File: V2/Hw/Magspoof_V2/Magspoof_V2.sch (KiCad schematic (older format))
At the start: 16 parts

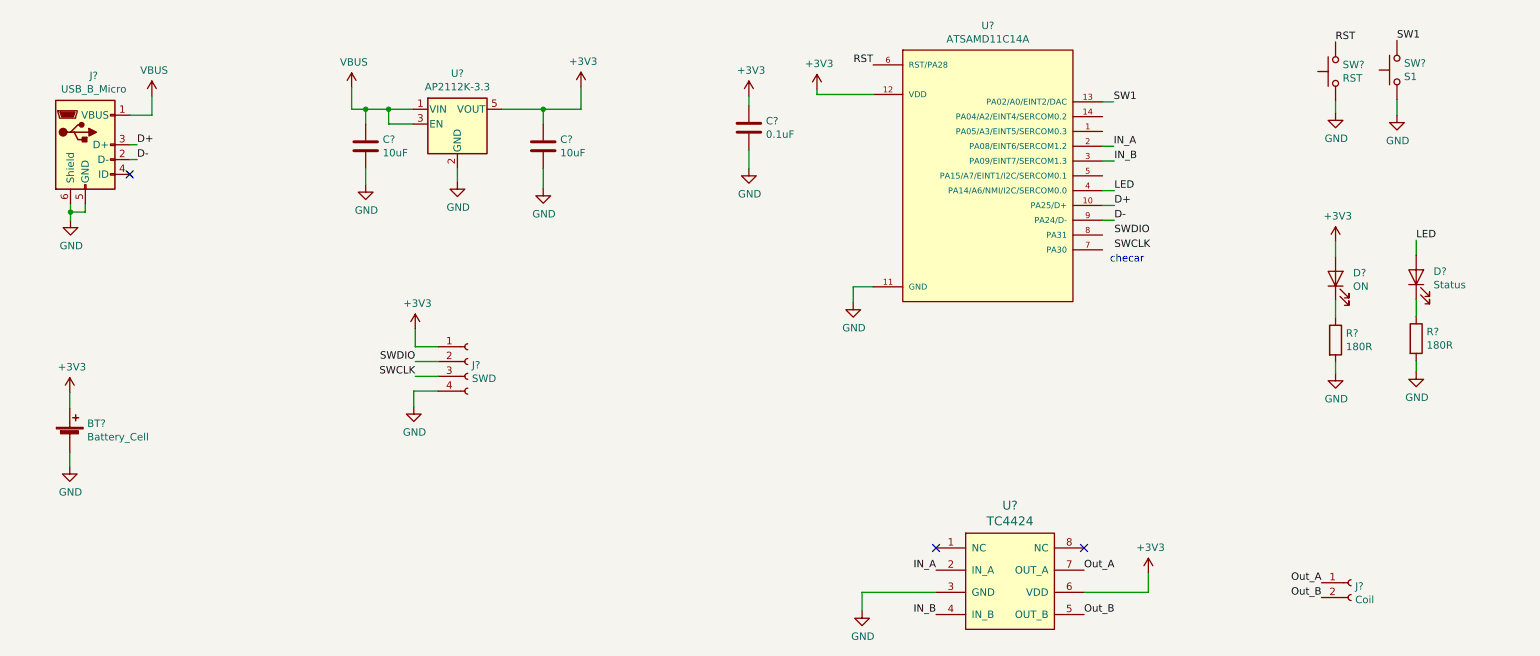
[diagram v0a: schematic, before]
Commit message: Add foortprints and first route
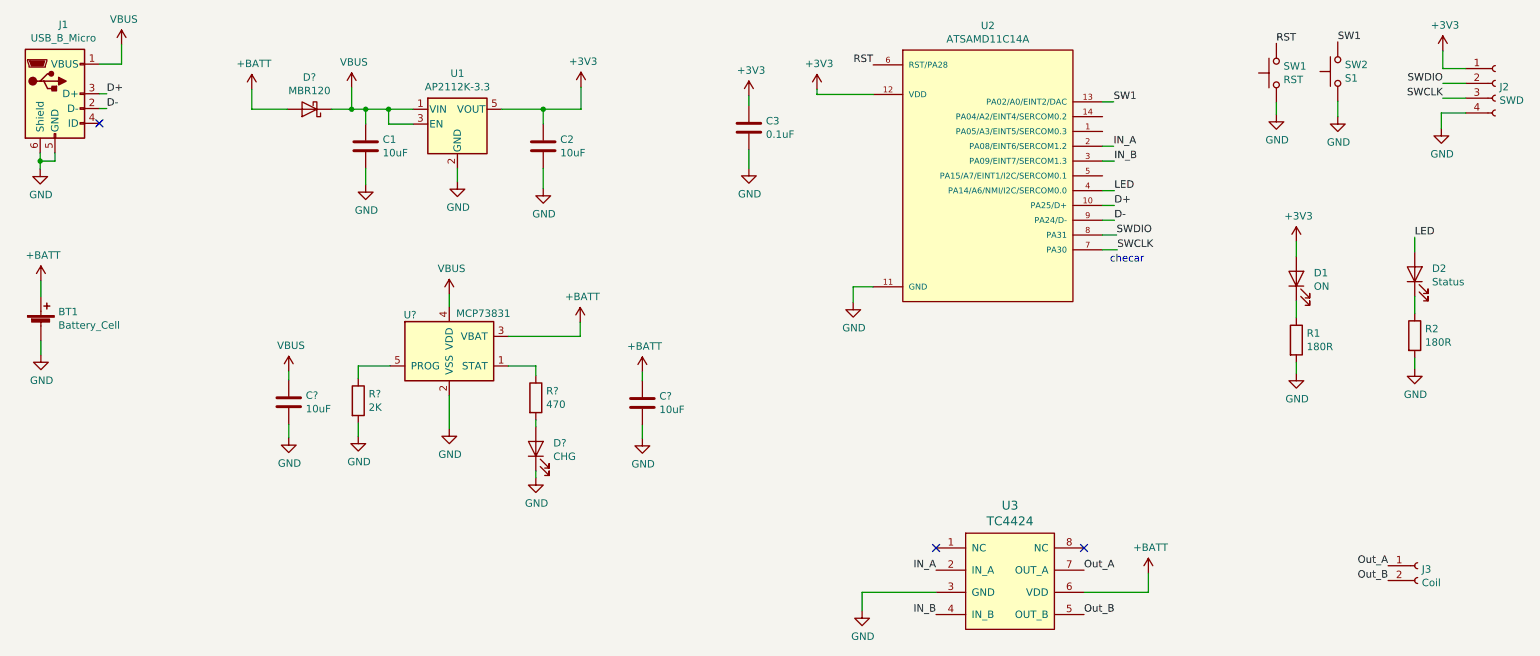
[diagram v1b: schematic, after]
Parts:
- added C? (x2): 10uF, Capacitor_SMD:C_0805_2012Metric_Pad1.15x1.40mm_HandSolder, symbol Device:C
- added D?: MBR120, Diode_SMD:D_SOD-123, symbol Device:D_Schottky
- added D?: CHG, LED_SMD:LED_0805_2012Metric_Pad1.15x1.40mm_HandSolder, symbol Device:LED
- added R?: 2K, Resistor_SMD:R_0805_2012Metric_Pad1.15x1.40mm_HandSolder, symbol Device:R
- added R?: 470, Resistor_SMD:R_0805_2012Metric_Pad1.15x1.40mm_HandSolder, symbol Device:R
- added U?: MCP73831, Package_TO_SOT_SMD:SOT-23-5, symbol Battery_Management:MCP73831-2-OT
- BT1: renamed from BT?; footprint (none) -> Connector_PinHeader_2.54mm:PinHeader_1x02_P2.54mm_Vertical
- C1, C2, C3: renamed from C?; footprint (none) -> Capacitor_SMD:C_0805_2012Metric_Pad1.15x1.40mm_HandSolder
- D1, D2: renamed from D?; footprint (none) -> LED_SMD:LED_0805_2012Metric_Pad1.15x1.40mm_HandSolder
- J1: renamed from J?; footprint (none) -> USB:629105150521
- J2: renamed from J?; footprint (none) -> Connector_PinHeader_2.54mm:PinHeader_1x04_P2.54mm_Vertical
- J3: renamed from J?; footprint (none) -> Connector_PinHeader_2.54mm:PinHeader_1x02_P2.54mm_Vertical
- R1, R2: renamed from R?; footprint (none) -> Resistor_SMD:R_0805_2012Metric_Pad1.15x1.40mm_HandSolder
- SW1, SW2: renamed from SW?; footprint (none) -> Button_Switch_SMD:SW_SPST_TL3342
- gave numbers to parts that had none: 3
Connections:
- net +3V3: no longer BT1.1 (+), U3.6 (VDD)
- net GND: now also C?.2, C?.2, D?.1 (K), R?.2, U?.2 (VSS)
- net SWCLK: now also U2.7 (PA30)
- net SWDIO: now also U2.8 (PA31)
- net VBUS: now also C?.1, D?.1 (K), U?.4 (VDD)
- new net: R?.1, U?.1 (STAT)
- new net: R?.1, U?.5 (PROG)
- new net: D?.2 (A), R?.2
- new net +BATT: BT1.1 (+), C?.1, D?.2 (A), U3.6 (VDD), U?.3 (VBAT)
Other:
- moved on the sheet: BT1, D1, D2, J1, J2, J3, R1, R2, SW1, SW2

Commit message: Update desing
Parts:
- added D5: MBR120, Diode_SMD:D_SOD-123, symbol Device:D_Schottky
- gave numbers to parts that had none: 7
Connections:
- net +BATT: now also D5.1 (K); no longer BT1.1 (+)
- new net: BT1.1 (+), D5.2 (A)
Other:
- moved on the sheet: BT1
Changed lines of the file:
@@
 L Device:Battery_Cell BT1
 U 1 1 5D60DD69
-P 960 2880
-F 0 "BT1" H 1078 2976 50  0000 L CNN
-F 1 "Battery_Cell" H 1078 2885 50  0000 L CNN
-F 2 "Connector_PinHeader_2.54mm:PinHeader_1x02_P2.54mm_Vertical" V 960 2940 50  0001 C CNN
-F 3 "~" V 960 2940 50  0001 C CNN
-	1    960  2880
+P 1030 3315
+F 0 "BT1" H 1148 3411 50  0000 L CNN
+F 1 "Battery_Cell" H 1148 3320 50  0000 L CNN
+F 2 "Connector_PinHeader_2.54mm:PinHeader_1x02_P2.54mm_Vertical" V 1030 3375 50  0001 C CNN
+F 3 "~" V 1030 3375 50  0001 C CNN
+	1    1030 3315
 	1    0    0    -1
 $EndComp
@@
 L power:GND #PWR0104
 U 1 1 5D62366E
-P 960 3075
-F 0 "#PWR0104" H 960 2825 50  0001 C CNN
-F 1 "GND" H 965 2902 50  0000 C CNN
-F 2 "" H 960 3075 50  0001 C CNN
-F 3 "" H 960 3075 50  0001 C CNN
-	1    960  3075
-	1    0    0    -1
-$EndComp
-Wire Wire Line
-	960  3075 960  2980
+P 1030 3510
+F 0 "#PWR0104" H 1030 3260 50  0001 C CNN
+F 1 "GND" H 1035 3337 50  0000 C CNN
+F 2 "" H 1030 3510 50  0001 C CNN
+F 3 "" H 1030 3510 50  0001 C CNN
+	1    1030 3510
+	1    0    0    -1
+$EndComp
+Wire Wire Line
+	1030 3510 1030 3415
 $Comp
 L power:GND #PWR0105
@@
 	4355 1950 4355 1815
 Wire Wire Line
-	960  2575 960  2680
+	1030 3010 1030 3115
 $Comp
 L power:+3V3 #PWR0112
@@
 	8230 2265 8135 2265
 $Comp
-L Battery_Management:MCP73831-2-OT U?
+L Battery_Management:MCP73831-2-OT U4
 U 1 1 5D644F3C
 P 3720 3050
-F 0 "U?" H 3455 3295 50  0000 C CNN
+F 0 "U4" H 3455 3295 50  0000 C CNN
 F 1 "MCP73831" H 3950 3305 50  0000 C CNN
 F 2 "Package_TO_SOT_SMD:SOT-23-5" H 3770 2800 50  0001 L CIN
@@
 $EndComp
 $Comp
-L power:+BATT #PWR?
+L power:+BATT #PWR0111
 U 1 1 5D647CAB
-P 960 2575
-F 0 "#PWR?" H 960 2425 50  0001 C CNN
-F 1 "+BATT" H 975 2748 50  0000 C CNN
-F 2 "" H 960 2575 50  0001 C CNN
-F 3 "" H 960 2575 50  0001 C CNN
-	1    960  2575
-	1    0    0    -1
-$EndComp
-$Comp
-L power:+BATT #PWR?
+P 1030 2650
+F 0 "#PWR0111" H 1030 2500 50  0001 C CNN
+F 1 "+BATT" H 1045 2823 50  0000 C CNN
+F 2 "" H 1030 2650 50  0001 C CNN
+F 3 "" H 1030 2650 50  0001 C CNN
+	1    1030 2650
+	1    0    0    -1
+$EndComp
+$Comp
+L power:+BATT #PWR0113
 U 1 1 5D649416
 P 4605 2855
-F 0 "#PWR?" H 4605 2705 50  0001 C CNN
+F 0 "#PWR0113" H 4605 2705 50  0001 C CNN
 F 1 "+BATT" H 4620 3028 50  0000 C CNN
 F 2 "" H 4605 2855 50  0001 C CNN
@@
 	4605 2950 4120 2950
 $Comp
-L Device:D_Schottky D?
+L Device:D_Schottky D3
 U 1 1 5D64EF3A
 P 2775 1415
-F 0 "D?" H 2775 1199 50  0000 C CNN
+F 0 "D3" H 2775 1199 50  0000 C CNN
 F 1 "MBR120" H 2775 1290 50  0000 C CNN
 F 2 "Diode_SMD:D_SOD-123" H 2775 1415 50  0001 C CNN
@@
 Connection ~ 3060 1415
 $Comp
-L power:+BATT #PWR?
+L power:+BATT #PWR0123
 U 1 1 5D6508CA
 P 2385 1280
-F 0 "#PWR?" H 2385 1130 50  0001 C CNN
+F 0 "#PWR0123" H 2385 1130 50  0001 C CNN
 F 1 "+BATT" H 2400 1453 50  0000 C CNN
 F 2 "" H 2385 1280 50  0001 C CNN
@@
 	2385 1415 2625 1415
 $Comp
-L power:+BATT #PWR?
+L power:+BATT #PWR0124
 U 1 1 5D6528AA
 P 8445 4550
-F 0 "#PWR?" H 8445 4400 50  0001 C CNN
+F 0 "#PWR0124" H 8445 4400 50  0001 C CNN
 F 1 "+BATT" H 8460 4723 50  0000 C CNN
 F 2 "" H 8445 4550 50  0001 C CNN
@@
 $EndComp
 $Comp
-L Device:R R?
+L Device:R R3
 U 1 1 5D6565D3
 P 3105 3385
-F 0 "R?" H 3175 3431 50  0000 L CNN
+F 0 "R3" H 3175 3431 50  0000 L CNN
 F 1 "2K" H 3175 3340 50  0000 L CNN
 F 2 "Resistor_SMD:R_0805_2012Metric_Pad1.15x1.40mm_HandSolder" V 3035 3385 50  0001 C CNN
@@
 	3105 3150 3105 3235
 $Comp
-L power:GND #PWR?
+L power:GND #PWR0125
 U 1 1 5D658144
 P 3720 3575
-F 0 "#PWR?" H 3720 3325 50  0001 C CNN
+F 0 "#PWR0125" H 3720 3325 50  0001 C CNN
 F 1 "GND" H 3725 3402 50  0000 C CNN
 F 2 "" H 3720 3575 50  0001 C CNN
@@
 	3720 3350 3720 3575
 $Comp
-L power:GND #PWR?
+L power:GND #PWR0126
 U 1 1 5D65A151
 P 3105 3625
-F 0 "#PWR?" H 3105 3375 50  0001 C CNN
+F 0 "#PWR0126" H 3105 3375 50  0001 C CNN
 F 1 "GND" H 3110 3452 50  0000 C CNN
 F 2 "" H 3105 3625 50  0001 C CNN
@@
 	3105 3625 3105 3535
 $Comp
-L power:VBUS #PWR?
+L power:VBUS #PWR0127
 U 1 1 5D65C1F4
 P 3720 2665
-F 0 "#PWR?" H 3720 2515 50  0001 C CNN
+F 0 "#PWR0127" H 3720 2515 50  0001 C CNN
 F 1 "VBUS" H 3735 2838 50  0000 C CNN
 F 2 "" H 3720 2665 50  0001 C CNN
@@
 	3720 2665 3720 2750
 $Comp
-L Device:C C?
+L Device:C C5
 U 1 1 5D65E6E6
 P 5025 3400
-F 0 "C?" H 5140 3446 50  0000 L CNN
+F 0 "C5" H 5140 3446 50  0000 L CNN
 F 1 "10uF" H 5140 3355 50  0000 L CNN
 F 2 "Capacitor_SMD:C_0805_2012Metric_Pad1.15x1.40mm_HandSolder" H 5063 3250 50  0001 C CNN
@@
 $EndComp
 $Comp
-L power:+BATT #PWR?
+L power:+BATT #PWR0128
 U 1 1 5D65F51F
 P 5025 3190
-F 0 "#PWR?" H 5025 3040 50  0001 C CNN
+F 0 "#PWR0128" H 5025 3040 50  0001 C CNN
 F 1 "+BATT" H 5040 3363 50  0000 C CNN
 F 2 "" H 5025 3190 50  0001 C CNN
@@
 	5025 3190 5025 3250
 $Comp
-L power:GND #PWR?
+L power:GND #PWR0129
 U 1 1 5D6612C8
 P 5025 3640
-F 0 "#PWR?" H 5025 3390 50  0001 C CNN
+F 0 "#PWR0129" H 5025 3390 50  0001 C CNN
 F 1 "GND" H 5030 3467 50  0000 C CNN
 F 2 "" H 5025 3640 50  0001 C CNN
@@
 	5025 3640 5025 3550
 $Comp
-L Device:C C?
+L Device:C C4
 U 1 1 5D66311C
 P 2635 3395
-F 0 "C?" H 2750 3441 50  0000 L CNN
+F 0 "C4" H 2750 3441 50  0000 L CNN
 F 1 "10uF" H 2750 3350 50  0000 L CNN
 F 2 "Capacitor_SMD:C_0805_2012Metric_Pad1.15x1.40mm_HandSolder" H 2673 3245 50  0001 C CNN
@@
 	2635 3185 2635 3245
 $Comp
-L power:GND #PWR?
+L power:GND #PWR0130
 U 1 1 5D663131
 P 2635 3635
-F 0 "#PWR?" H 2635 3385 50  0001 C CNN
+F 0 "#PWR0130" H 2635 3385 50  0001 C CNN
 F 1 "GND" H 2640 3462 50  0000 C CNN
 F 2 "" H 2635 3635 50  0001 C CNN
@@
 	2635 3635 2635 3545
 $Comp
-L power:VBUS #PWR?
+L power:VBUS #PWR0131
 U 1 1 5D665A07
 P 2635 3185
-F 0 "#PWR?" H 2635 3035 50  0001 C CNN
+F 0 "#PWR0131" H 2635 3035 50  0001 C CNN
 F 1 "VBUS" H 2650 3358 50  0000 C CNN
 F 2 "" H 2635 3185 50  0001 C CNN
@@
 $EndComp
 $Comp
-L Device:LED D?
+L Device:LED D4
 U 1 1 5D6777EB
 P 4305 3710
-F 0 "D?" V 4344 3592 50  0000 R CNN
+F 0 "D4" V 4344 3592 50  0000 R CNN
 F 1 "CHG" V 4253 3592 50  0000 R CNN
 F 2 "LED_SMD:LED_0805_2012Metric_Pad1.15x1.40mm_HandSolder" H 4305 3710 50  0001 C CNN
@@
 $EndComp
 $Comp
-L power:GND #PWR?
+L power:GND #PWR0132
 U 1 1 5D67FC05
 P 4305 3905
-F 0 "#PWR?" H 4305 3655 50  0001 C CNN
+F 0 "#PWR0132" H 4305 3655 50  0001 C CNN
 F 1 "GND" H 4310 3732 50  0000 C CNN
 F 2 "" H 4305 3905 50  0001 C CNN
@@
 $EndComp
 $Comp
-L Device:R R?
+L Device:R R4
 U 1 1 5D6809EB
 P 4305 3365
-F 0 "R?" H 4375 3411 50  0000 L CNN
+F 0 "R4" H 4375 3411 50  0000 L CNN
 F 1 "470" H 4375 3320 50  0000 L CNN
 F 2 "Resistor_SMD:R_0805_2012Metric_Pad1.15x1.40mm_HandSolder" V 4235 3365 50  0001 C CNN
@@
 Wire Wire Line
 	4305 3860 4305 3905
+$Comp
+L Device:D_Schottky D5
+U 1 1 5D64C04E
+P 1030 2860
+F 0 "D5" H 1030 2644 50  0000 C CNN
+F 1 "MBR120" H 1030 2735 50  0000 C CNN
+F 2 "Diode_SMD:D_SOD-123" H 1030 2860 50  0001 C CNN
+F 3 "~" H 1030 2860 50  0001 C CNN
+	1    1030 2860
+	0    1    1    0
+$EndComp
+Wire Wire Line
+	1030 2650 1030 2710
 $EndSCHEMATC
